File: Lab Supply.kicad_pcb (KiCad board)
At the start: 2 copper layers, 182.9 x 111.8 mm, 17 parts, among them Q1 NPN, U1 LM358, U2 LM358

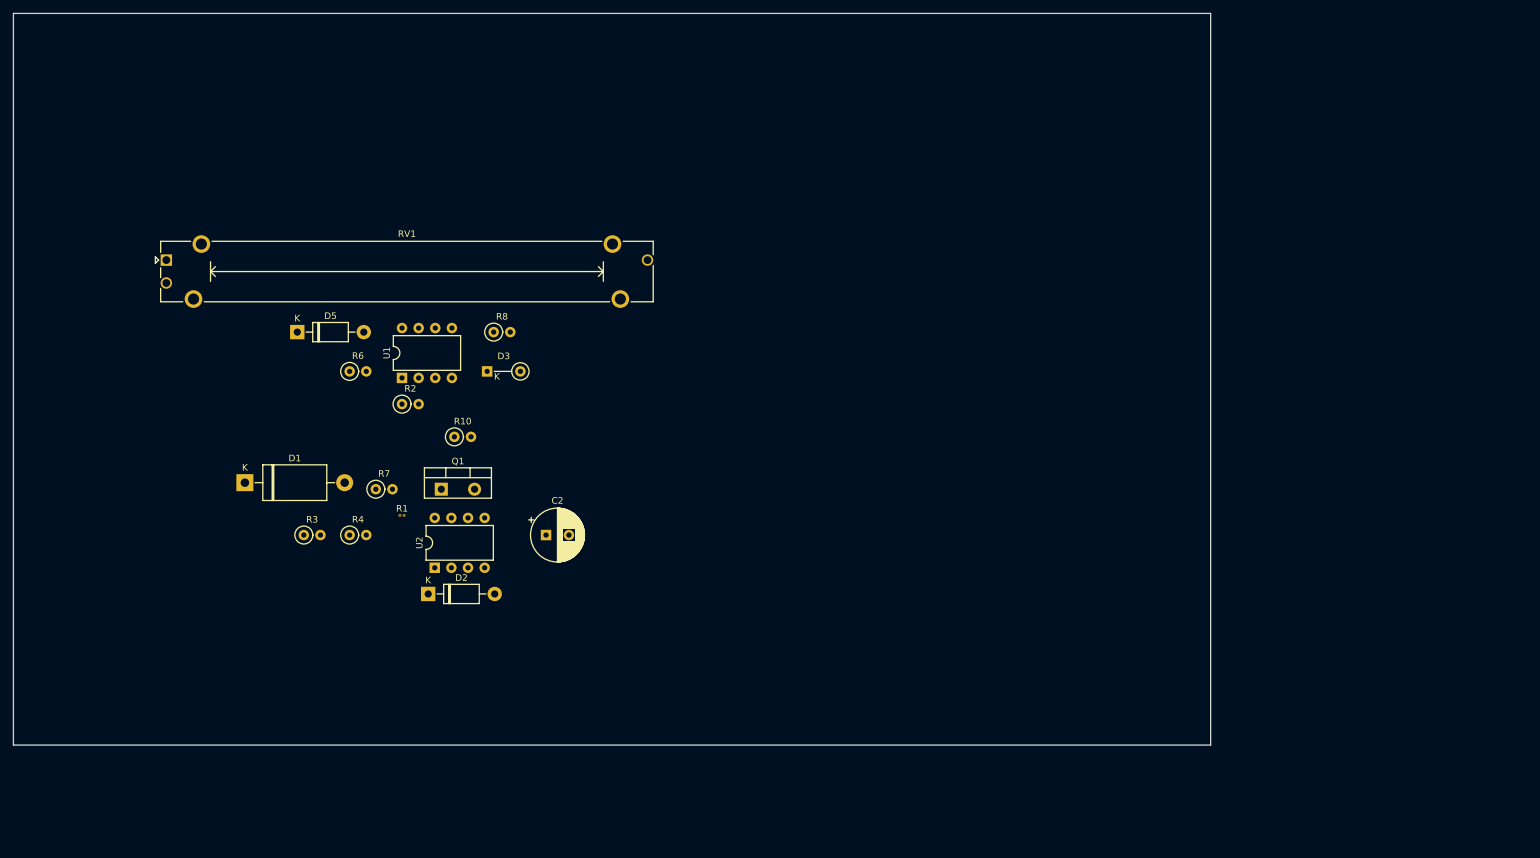
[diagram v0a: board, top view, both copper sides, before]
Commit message: Changed to LM324
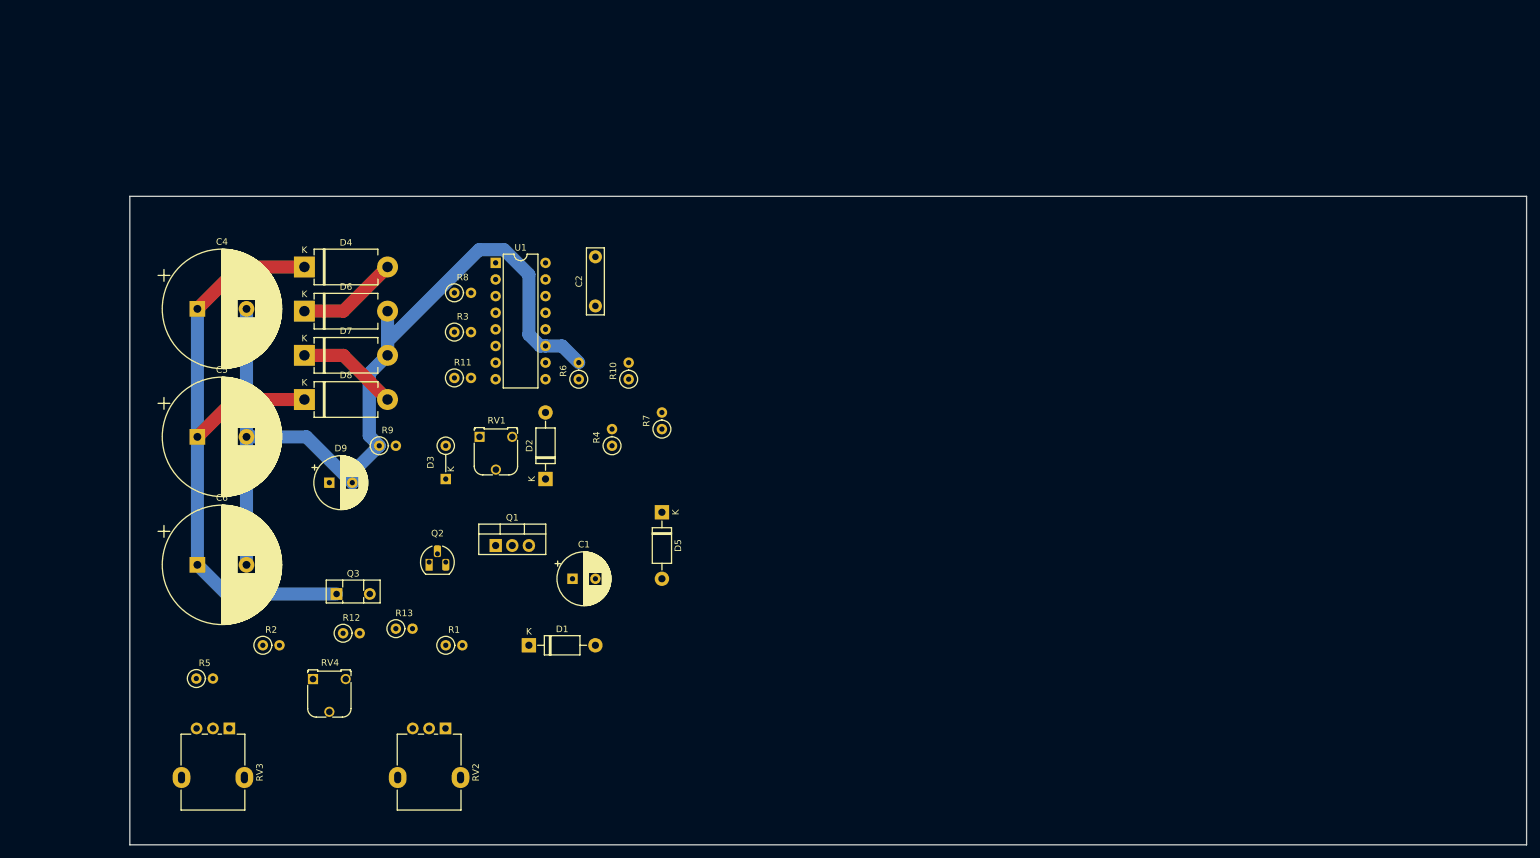
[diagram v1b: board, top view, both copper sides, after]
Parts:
- removed U2: LM358, Package_DIP:DIP-8_W7.62mm
- added C1: 100u, Capacitor_THT:CP_Radial_D8.0mm_P3.50mm, F.Cu at (126.0, 106.7)
- added C4: 4700u, Capacitor_THT:CP_Radial_D18.0mm_P7.50mm, F.Cu at (68.7, 65.5)
- added C5: 4700u, Capacitor_THT:CP_Radial_D18.0mm_P7.50mm, F.Cu at (68.7, 85.0)
- added C6: 4700u, Capacitor_THT:CP_Radial_D18.0mm_P7.50mm, F.Cu at (68.7, 104.5)
- added D4: 1N5400, Diode_THT:D_DO-201AD_P12.70mm_Horizontal, F.Cu at (85.1, 59.0)
- added D6: 1N5400, Diode_THT:D_DO-201AD_P12.70mm_Horizontal, F.Cu at (85.1, 65.8)
- added D7: 1N5400, Diode_THT:D_DO-201AD_P12.70mm_Horizontal, F.Cu at (85.1, 72.5)
- added D8: 1N5400, Diode_THT:D_DO-201AD_P12.70mm_Horizontal, F.Cu at (85.1, 79.3)
- added D9: 1N4751ATR, Capacitor_THT:CP_Radial_D8.0mm_P3.50mm, F.Cu at (88.9, 92.0)
- added Q2: 2N2222, Package_TO_SOT_THT:TO-92_HandSolder, F.Cu at (104.1, 104.1)
- added Q3: TIP121, Package_TO_SOT_THT:TO-126-2_Vertical, F.Cu at (90.0, 109.0)
- added R11: 4.7k, Resistor_THT:R_Axial_DIN0207_L6.3mm_D2.5mm_P2.54mm_Vertical, F.Cu at (108.0, 76.0)
- added R12: 10k, Resistor_THT:R_Axial_DIN0207_L6.3mm_D2.5mm_P2.54mm_Vertical, F.Cu at (91.0, 115.0)
- added R13: 100, Resistor_THT:R_Axial_DIN0207_L6.3mm_D2.5mm_P2.54mm_Vertical, F.Cu at (99.1, 114.3)
- added R5: 47k, Resistor_THT:R_Axial_DIN0207_L6.3mm_D2.5mm_P2.54mm_Vertical, F.Cu at (68.6, 121.9)
- added R9: 4.7k, Resistor_THT:R_Axial_DIN0207_L6.3mm_D2.5mm_P2.54mm_Vertical, F.Cu at (96.5, 86.4)
- added RV2: 1k, Potentiometer_THT:Potentiometer_Alpha_RD901F-40-00D_Single_Vertical, F.Cu at (106.6, 129.5)
- added RV3: 10k, Potentiometer_THT:Potentiometer_Alpha_RD901F-40-00D_Single_Vertical, F.Cu at (73.6, 129.5)
- added RV4: 10k, Potentiometer_THT:Potentiometer_Runtron_RM-065_Vertical, F.Cu at (86.4, 122.0)
- C2: footprint Capacitor_THT:CP_Radial_D8.0mm_P3.50mm -> Capacitor_THT:C_Rect_L10.0mm_W2.5mm_P7.50mm_MKS4
- D1: footprint Diode_THT:D_DO-201_P15.24mm_Horizontal -> Diode_THT:D_DO-41_SOD81_P10.16mm_Horizontal
- D3: value I LIMIT -> I_LIMIT_ON
- Q1: value NPN -> TIP121; footprint Package_TO_SOT_THT:TO-220-2_Vertical -> Package_TO_SOT_THT:TO-220-3_Vertical
- R1: footprint Resistor_SMD:R_0201_0603Metric -> Resistor_THT:R_Axial_DIN0207_L6.3mm_D2.5mm_P2.54mm_Vertical
- R2: value 22k -> 3.9k
- R6: value 0.05 -> 0.5
- RV1: footprint Potentiometer_THT:Potentiometer_Bourns_PTA6043_Single_Slide -> Potentiometer_THT:Potentiometer_Runtron_RM-065_Vertical
- U1: value LM358 -> LM324; footprint Package_DIP:DIP-8_W7.62mm -> Package_DIP:DIP-16_W7.62mm
- moved D5 62.1 mm to (139.7, 96.5), turned to -90 degrees
- moved RV1 54.9 mm to (111.8, 85.0)
- moved D1 50.0 mm to (119.4, 116.8)
- moved R7 44.7 mm to (139.7, 83.8), turned to 90 degrees
- moved R2 42.5 mm to (78.7, 116.8)
- moved R4 42.3 mm to (132.1, 86.4), turned to 90 degrees
- moved R3 38.6 mm to (108.0, 69.0)
- moved C2 35.8 mm to (129.5, 65.0), turned to 90 degrees
- moved R6 35.0 mm to (127.0, 76.2), turned to 90 degrees
- moved R10 28.0 mm to (134.6, 76.2), turned to 90 degrees
- moved D2 25.1 mm to (121.9, 91.4), turned to 90 degrees
- moved U1 22.7 mm to (114.3, 58.4), turned to 0 degrees
- moved R1 20.9 mm to (106.7, 116.8)
- moved D3 17.6 mm to (106.7, 91.4), turned to 90 degrees
- moved Q1 12.0 mm to (114.3, 101.6)
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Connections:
- C2 pad 1: Net-(U2B--) -> Net-(U1D--)
- Q1 pad 1: +36V -> Net-(Q1-C)
- Q1 pad 2: Net-(Q1-B) -> Net-(D2-A)
- R1 pad 1: +36V -> Net-(Q1-C)
- R10 pad 2: Net-(Q1-B) -> Net-(D2-A)
- R3 pad 2: Net-(U2B--) -> Net-(U1D--)
- R4 pad 1: Net-(U2B--) -> Net-(U1D--)
- U1 pad 4: GND -> +36V
- U1 pad 8: +36V -> Net-(D2-K)
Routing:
- net GND: track 0.00 -> 137.5 mm
- net +36V: track 0.00 -> 99.9 mm
- net Net-(D7-K): track 0.00 -> 15.5 mm
- net Net-(D4-A): track 0.00 -> 15.5 mm
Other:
- board size 182.9 x 111.8 mm -> 213.4 x 99.1 mm

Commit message: Started working on firmware
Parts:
- removed D1: 1N5919BG, Diode_THT:D_DO-41_SOD81_P10.16mm_Horizontal
- removed RV1: 10k, Potentiometer_THT:Potentiometer_Runtron_RM-065_Vertical
- removed RV2: 1k, Potentiometer_THT:Potentiometer_Alpha_RD901F-40-00D_Single_Vertical
- added C3: 100n, Capacitor_THT:C_Rect_L4.0mm_W2.5mm_P2.50mm, F.Cu at (180.3, 96.5)
- added C8: 100n, Capacitor_THT:C_Rect_L4.0mm_W2.5mm_P2.50mm, F.Cu at (172.8, 129.5)
- added D11: 1N4001, Diode_THT:D_DO-41_SOD81_P10.16mm_Horizontal, F.Cu at (114.3, 81.3)
- added H1: LCD, Arduino:Display Header, F.Cu at (198.1, 142.2)
- added M1: Fan_4pin, Connector:FanPinHeader_1x04_P2.54mm_Vertical, F.Cu at (184.2, 142.2)
- added Q4: 2N3904, Package_TO_SOT_THT:TO-92_HandSolder, F.Cu at (196.8, 97.8)
- added Q5: 2N3904, Package_TO_SOT_THT:TO-92_HandSolder, F.Cu at (111.8, 132.1)
- added R14: 22k, Resistor_THT:R_Axial_DIN0207_L6.3mm_D2.5mm_P2.54mm_Vertical, F.Cu at (270.5, 129.3)
- added R15: 10k, Resistor_THT:R_Axial_DIN0207_L6.3mm_D2.5mm_P2.54mm_Vertical, F.Cu at (190.5, 111.8)
- added R16: 100k, Resistor_THT:R_Axial_DIN0207_L6.3mm_D2.5mm_P2.54mm_Vertical, F.Cu at (233.7, 117.1)
- added R17: 10k, Resistor_THT:R_Axial_DIN0207_L6.3mm_D2.5mm_P2.54mm_Vertical, F.Cu at (91.4, 106.7)
- added R18: 10k, Resistor_THT:R_Axial_DIN0207_L6.3mm_D2.5mm_P2.54mm_Vertical, F.Cu at (256.5, 86.4)
- added R19: 10k, Resistor_THT:R_Axial_DIN0207_L6.3mm_D2.5mm_P2.54mm_Vertical, F.Cu at (210.8, 96.5)
- added R20: 4.7k, Resistor_THT:R_Axial_DIN0207_L6.3mm_D2.5mm_P2.54mm_Vertical, F.Cu at (188.0, 99.1)
- added RV5: 200k, Potentiometer_THT:Potentiometer_Bourns_3339H_Vertical, F.Cu at (238.2, 82.6)
- added RV6: 20k, Potentiometer_THT:Potentiometer_Bourns_3339H_Vertical, F.Cu at (238.2, 91.8)
- added RV7: 10k, Potentiometer_THT:Potentiometer_Bourns_3339H_Vertical, F.Cu at (238.2, 101.1)
- added U2: LM7812_TO220, Package_TO_SOT_THT:TO-220-3_Vertical, F.Cu at (170.2, 139.7)
- added U3: MCP4922, Package_DIP:DIP-14_W7.62mm, F.Cu at (177.8, 104.1)
- added U4: LM7805_TO220, Package_TO_SOT_THT:TO-220-3_Vertical, F.Cu at (221.0, 111.8)
- added U5: LM4040DBZ-2.0, Package_TO_SOT_THT:TO-92_HandSolder, F.Cu at (181.6, 129.5)
- added U6: MCP3202, Package_DIP:DIP-8_W7.62mm, F.Cu at (204.5, 108.0)
- added U7: ~, Arduino:Itsy Bitsy 5V, F.Cu at (218.4, 127.0)
- C1: footprint Capacitor_THT:CP_Radial_D8.0mm_P3.50mm -> Capacitor_THT:C_Axial_L3.8mm_D2.6mm_P7.50mm_Horizontal
- C2: footprint Capacitor_THT:C_Rect_L10.0mm_W2.5mm_P7.50mm_MKS4 -> Capacitor_THT:C_Rect_L4.0mm_W2.5mm_P2.50mm
- D9: footprint Capacitor_THT:CP_Radial_D8.0mm_P3.50mm -> Diode_THT:D_DO-41_SOD81_P10.16mm_Horizontal
- Q2: value 2N2222 -> 2N3904
- Q3: footprint Package_TO_SOT_THT:TO-126-2_Vertical -> Package_TO_SOT_THT:TO-220-3_Vertical
- R1: value 10k -> 1k
- R2: value 3.9k -> 47k
- R4: value 47k -> 68k
- R5: value 47k -> 10k
- RV3: value 10k -> 22k; footprint Potentiometer_THT:Potentiometer_Alpha_RD901F-40-00D_Single_Vertical -> Potentiometer_THT:Potentiometer_Bourns_3339H_Vertical
- RV4: footprint Potentiometer_THT:Potentiometer_Runtron_RM-065_Vertical -> Potentiometer_THT:Potentiometer_Bourns_3339H_Vertical
- moved RV3 177.1 mm to (238.2, 64.1), turned to 0 degrees
- moved RV4 159.4 mm to (238.2, 73.3)
- moved R1 112.5 mm to (218.4, 104.1), turned to 180 degrees
- moved R2 111.8 mm to (190.5, 119.4)
- moved R4 91.5 mm to (223.5, 88.9), turned to 0 degrees
- moved R8 66.7 mm to (132.1, 125.2)
- moved D4 63.4 mm to (68.6, 120.2)
- moved D6 63.4 mm to (68.6, 127.0)
- moved D7 63.4 mm to (68.6, 133.8)
- moved D8 63.4 mm to (68.6, 140.5)
- moved R6 45.8 mm to (124.5, 121.9), turned to 0 degrees
- moved Q2 39.9 mm to (97.8, 64.8)
- moved D9 37.6 mm to (91.4, 129.5)
- moved D5 35.3 mm to (109.2, 114.3), turned to 0 degrees
- moved R7 34.1 mm to (124.5, 114.3), turned to 0 degrees
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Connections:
- net Net-(D5-K) renamed V+
- C1 pad 2: Net-(D1-A) -> ISENSE
- D2 pad 2: Net-(D2-A) -> Net-(D11-A)
- D5 pad 2: Net-(D1-A) -> ISENSE
- Q1 pad 1: Net-(Q1-C) -> +28V
- Q1 pad 2: Net-(D2-A) -> Net-(D11-A)
- Q2 pad 1: Net-(Q2-C) -> Net-(D11-K)
- R1 pad 1: Net-(Q1-C) -> +5V
- R1 pad 2: Net-(D1-K) -> VREF
- R10 pad 2: Net-(D2-A) -> Net-(D11-A)
- R11 pad 2: Net-(D1-A) -> ISENSE
- R2 pad 1: Net-(R2-Pad1) -> V_ISET
- R2 pad 2: Net-(U1A--) -> Net-(U1C-+)
- R3 pad 1: Net-(D1-A) -> ISENSE
- R4 pad 1: Net-(U1D--) -> Net-(R4-Pad1)
- R5 pad 1: Net-(Q2-C) -> Net-(U1B--)
- R5 pad 2: Net-(R5-Pad2) -> GND
- R6 pad 1: Net-(D1-A) -> ISENSE
- R7 pad 2: Net-(D1-A) -> ISENSE
- R8 pad 1: Net-(R8-Pad1) -> Net-(Q5-E)
- RV3 pad 1: Net-(U1A--) -> unconnected-(RV3-Pad1)
- RV3 pad 2: Net-(R5-Pad2) -> Net-(R15-Pad2)
- RV3 pad 3: Net-(D1-A) -> GND
- RV4 pad 1: Net-(R2-Pad1) -> Net-(U6-CH1)
- U1 pad 1: Net-(U1A--) -> Net-(R17-Pad2)
- U1 pad 12: Net-(Q2-C) -> V_VSET
- U1 pad 2: Net-(U1A--) -> Net-(D2-K)
- U1 pad 3: Net-(U1A-+) -> Net-(D11-A)
- U1 pad 4: +36V -> +28V
- U1 pad 5: Net-(U1A--) -> ISENSE
- U1 pad 6: Net-(D2-K) -> Net-(U1B--)
- U1 pad 7: Net-(R8-Pad1) -> Net-(U6-CH0)
- U1 pad 9: Net-(D1-A) -> ISENSE
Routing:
- net GND: track 137.5 -> 0.00 mm
- net +36V: track 99.9 -> 0.00 mm
- net Net-(D7-K): track 15.5 -> 0.00 mm
- net Net-(D4-A): track 15.5 -> 0.00 mm

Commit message: WIP
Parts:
- removed H1: LCD, Arduino:Display Header
- removed Q4: 2N3904, Package_TO_SOT_THT:TO-92_HandSolder
- removed RV7: 10k, Potentiometer_THT:Potentiometer_Bourns_3339H_Vertical
- added C10: 100n, Capacitor_THT:C_Rect_L10.0mm_W2.5mm_P7.50mm_MKS4, F.Cu at (116.8, 55.9)
- added C11: 100u, Capacitor_THT:CP_Radial_D8.0mm_P3.50mm, F.Cu at (106.7, 97.5)
- added C12: 100n, Capacitor_THT:C_Rect_L10.0mm_W2.5mm_P7.50mm_MKS4, F.Cu at (102.9, 119.4)
- added C13: 10u, Capacitor_THT:C_Rect_L10.0mm_W2.5mm_P7.50mm_MKS4, F.Cu at (121.9, 72.3)
- added C15: 100n, Capacitor_THT:C_Rect_L10.0mm_W2.5mm_P7.50mm_MKS4, F.Cu at (127.0, 114.3)
- added C16: 10u, Capacitor_THT:C_Rect_L10.0mm_W2.5mm_P7.50mm_MKS4, F.Cu at (133.4, 132.1)
- added C9: 100n, Capacitor_THT:C_Rect_L10.0mm_W2.5mm_P7.50mm_MKS4, F.Cu at (151.2, 86.4)
- added D10: 1N4001, Diode_THT:D_DO-41_SOD81_P10.16mm_Horizontal, F.Cu at (129.5, 96.5)
- added D12: 1N4001, Diode_THT:D_DO-41_SOD81_P10.16mm_Horizontal, F.Cu at (157.5, 78.7)
- added R19: 10k, Resistor_THT:R_Axial_DIN0204_L3.6mm_D1.6mm_P7.62mm_Horizontal, F.Cu at (119.4, 80.0)
- added R21: 100, Resistor_THT:R_Axial_DIN0204_L3.6mm_D1.6mm_P7.62mm_Horizontal, F.Cu at (139.0, 99.0)
- added R22: 100, Resistor_THT:R_Axial_DIN0204_L3.6mm_D1.6mm_P7.62mm_Horizontal, F.Cu at (110.0, 55.0)
- added R23: 470, Resistor_THT:R_Axial_DIN0204_L3.6mm_D1.6mm_P7.62mm_Horizontal, F.Cu at (134.6, 111.8)
- added R24: 470, Resistor_THT:R_Axial_DIN0204_L3.6mm_D1.6mm_P7.62mm_Horizontal, F.Cu at (137.2, 121.9)
- added R25: 470, Resistor_THT:R_Axial_DIN0204_L3.6mm_D1.6mm_P7.62mm_Horizontal, F.Cu at (147.3, 81.3)
- C1: footprint Capacitor_THT:C_Axial_L3.8mm_D2.6mm_P7.50mm_Horizontal -> Capacitor_THT:CP_Radial_D8.0mm_P3.50mm
- C2, C3, C8: footprint Capacitor_THT:C_Rect_L4.0mm_W2.5mm_P2.50mm -> Capacitor_THT:C_Rect_L10.0mm_W2.5mm_P7.50mm_MKS4
- D5: value 1N4001 -> 1N5400; footprint Diode_THT:D_DO-41_SOD81_P10.16mm_Horizontal -> Diode_THT:D_DO-201AD_P12.70mm_Horizontal
- M1: footprint Connector:FanPinHeader_1x04_P2.54mm_Vertical -> Connector_FFC-FPC:Molex_200528-0040_1x04-1MP_P1.00mm_Horizontal
- R1, R10, R12, R13, R14, R15, R16, R17, R18, R2, R3, R4, R5, R7, R8: footprint Resistor_THT:R_Axial_DIN0207_L6.3mm_D2.5mm_P2.54mm_Vertical -> Resistor_THT:R_Axial_DIN0204_L3.6mm_D1.6mm_P7.62mm_Horizontal
- R11: value 4.7k -> 10k; footprint Resistor_THT:R_Axial_DIN0207_L6.3mm_D2.5mm_P2.54mm_Vertical -> Resistor_THT:R_Axial_DIN0204_L3.6mm_D1.6mm_P7.62mm_Horizontal
- R20: value 4.7k -> 100; footprint Resistor_THT:R_Axial_DIN0207_L6.3mm_D2.5mm_P2.54mm_Vertical -> Resistor_THT:R_Axial_DIN0204_L3.6mm_D1.6mm_P7.62mm_Horizontal
- R6: footprint Resistor_THT:R_Axial_DIN0207_L6.3mm_D2.5mm_P2.54mm_Vertical -> Resistor_THT:R_Axial_Power_L20.0mm_W6.4mm_P25.40mm
- R9: value 4.7k -> 22k; footprint Resistor_THT:R_Axial_DIN0207_L6.3mm_D2.5mm_P2.54mm_Vertical -> Resistor_THT:R_Axial_DIN0204_L3.6mm_D1.6mm_P7.62mm_Horizontal
- moved Q1 127.9 mm to (233.7, 106.7), turned to 180 degrees
- moved R14 124.8 mm to (160.0, 71.1)
- moved M1 123.8 mm to (99.8, 51.5)
- moved U4 123.1 mm to (106.7, 66.0)
- moved R18 114.1 mm to (144.0, 105.0)
- moved D2 112.2 mm to (210.8, 91.4), turned to 90 degrees
- moved R11 110.9 mm to (193.0, 109.2), turned to 90 degrees
- moved R7 104.4 mm to (228.6, 121.9), turned to 90 degrees
- moved Q2 103.6 mm to (181.6, 125.7), turned to 180 degrees
- moved RV4 103.6 mm to (135.4, 85.6)
- moved D3 102.0 mm to (214.0, 53.3)
- moved R9 100.7 mm to (193.0, 119.4), turned to -90 degrees
- moved D5 99.5 mm to (208.3, 105.4), turned to -90 degrees
- moved C2 98.2 mm to (208.4, 66.0)
- moved C8 91.7 mm to (99.1, 75.0), turned to -90 degrees
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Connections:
- M1 pad 1: GND -> unconnected-(M1---Pad1)
- M1 pad 4: Net-(M1-PWM) -> unconnected-(M1-PWM-Pad4)
- R1 pad 2: VREF -> Net-(U5-A)
- R14 pad 2: Net-(U6-CH0) -> Net-(R14-Pad2)
- R20 pad 1: ACD/~{DAC} -> Net-(U6-~{CS}/SHDN)
- R20 pad 2: Net-(Q4-B) -> Net-(U7-A5)
- U1 pad 7: Net-(U6-CH0) -> Net-(R14-Pad2)
- U3 pad 3: ACD/~{DAC} -> unconnected-(U3-~{CS}-Pad3)
- U3 pad 8: unconnected-(U3-~{LDAC}-Pad8) -> GND
- U3 pad 9: GND -> +5V
- U5 pad 2: VREF -> Net-(U5-A)
- U6 pad 1: Net-(Q4-C) -> Net-(U6-~{CS}/SHDN)
- U6 pad 2: Net-(U6-CH0) -> Net-(D10-A)
- U6 pad 5: Net-(U3-SDI) -> Net-(U6-DIN)
- U6 pad 7: Net-(U3-SCK) -> Net-(U6-CLK)
- U6 pad 8: VREF -> Net-(U5-A)
- U7 pad 10: Net-(H1-DB4) -> Net-(U7-A5)
- U7 pad 17: Net-(M1-PWM) -> unconnected-(U7-D6-Pad17)
- U7 pad 19: Net-(H1-DB3) -> unconnected-(U7-D0-Pad19)
- U7 pad 20: Net-(H2-CLK) (its old number) -> unconnected-(U7-D1-Pad20)
- U7 pad 21: Net-(H2-DT) (its old number) -> unconnected-(U7-SDA-Pad21)
- U7 pad 22: Net-(H2-SW) (its old number) -> unconnected-(U7-SCL-Pad22)
- U7 pad 7: Net-(H3-SW) -> unconnected-(U7-A2-Pad7)
- U7 pad 8: Net-(H3-DT) -> unconnected-(U7-A3-Pad8)
- U7 pad 9: Net-(H3-CLK) -> unconnected-(U7-A4-Pad9)
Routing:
- net GND: track 0.00 -> 234.7 mm
- net +28V: track 0.00 -> 170.2 mm
- net +36V: track 0.00 -> 117.8 mm
- net V+: track 0.00 -> 20.8 mm
- net Net-(D7-K): track 0.00 -> 15.5 mm
- net Net-(D4-A): track 0.00 -> 15.5 mm
- net ISENSE: track 0.00 -> 14.0 mm
- net (no net): vias 0 -> 1
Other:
- board size 213.4 x 99.1 mm -> 213.4 x 104.1 mm

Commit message: Rearranged firmware code
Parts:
- removed the R19 at (193.0, 88.9)
- added CONN1: V+, Connector_Wire:SolderWire-1.5sqmm_1x01_D1.7mm_OD3.9mm, F.Cu at (444.5, 134.6)
- added CONN2: V-, Connector_Wire:SolderWire-1.5sqmm_1x01_D1.7mm_OD3.9mm, F.Cu at (444.5, 160.0)
- added CONN3: AC1, Connector_Wire:SolderWire-1.5sqmm_1x01_D1.7mm_OD3.9mm, F.Cu at (57.1, 124.5)
- added CONN4: AC2, Connector_Wire:SolderWire-1.5sqmm_1x01_D1.7mm_OD3.9mm, F.Cu at (57.1, 134.6)
- added H1: Current, Arduino:5 Pin Header, F.Cu at (381.0, 76.2)
- added H2: Voltage, Arduino:5 Pole Header, F.Cu at (388.6, 76.2)
- added SW1: ENABLE, Arduino:2 Pin Header, F.Cu at (381.0, 157.5)
- C13, C16: footprint Capacitor_THT:C_Rect_L10.0mm_W2.5mm_P7.50mm_MKS4 -> Capacitor_THT:CP_Radial_D8.0mm_P3.50mm
- M1: footprint Connector_FFC-FPC:Molex_200528-0040_1x04-1MP_P1.00mm_Horizontal -> Connector_Molex:Molex_KK-254_AE-6410-04A_1x04_P2.54mm_Vertical
- U1: footprint Package_DIP:DIP-16_W7.62mm -> Package_DIP:DIP-14_W7.62mm
- moved C1 292.4 mm to (413.1, 139.7)
- moved U6 240.0 mm to (370.8, 55.9)
- moved R22 233.0 mm to (340.4, 90.2), turned to 90 degrees
- moved M1 228.8 mm to (317.5, 121.9)
- moved U3 214.6 mm to (358.1, 76.2)
- moved R16 214.4 mm to (373.4, 137.2), turned to 90 degrees
- moved R20 213.5 mm to (345.4, 147.3)
- moved D10 213.4 mm to (342.9, 101.6)
- moved R23 212.2 mm to (342.9, 152.4), turned to 180 degrees
- moved U4 208.8 mm to (315.0, 81.3)
- moved R24 208.3 mm to (345.4, 127.0)
- moved C10 205.9 mm to (318.7, 96.5), turned to 180 degrees
- moved R19 205.1 mm to (323.9, 96.5), turned to 0 degrees
- moved R11 202.6 mm to (393.7, 137.2)
- moved C15 201.8 mm to (325.1, 152.4)
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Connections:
- net Net-(D4-A) renamed AC1
- net Net-(D7-K) renamed AC2
- C16 pad 1: Net-(U5-A) -> GND
- C16 pad 2: GND -> Net-(U5-A)
- M1 pad 1: unconnected-(M1---Pad1) -> GND
- M1 pad 4: unconnected-(M1-PWM-Pad4) -> Net-(M1-PWM)
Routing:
- net GND: track 234.7 -> 0.00 mm
- net +28V: track 170.2 -> 0.00 mm
- net +36V: track 117.8 -> 0.00 mm
- net V+: track 20.8 -> 0.00 mm
- net AC2: track 15.5 -> 0.00 mm
- net AC1: track 15.5 -> 0.00 mm
- net ISENSE: track 14.0 -> 0.00 mm
- net (no net): vias 1 -> 0
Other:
- board size 213.4 x 104.1 mm -> 198.1 x 116.8 mm
